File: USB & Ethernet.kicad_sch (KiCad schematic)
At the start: 17 parts

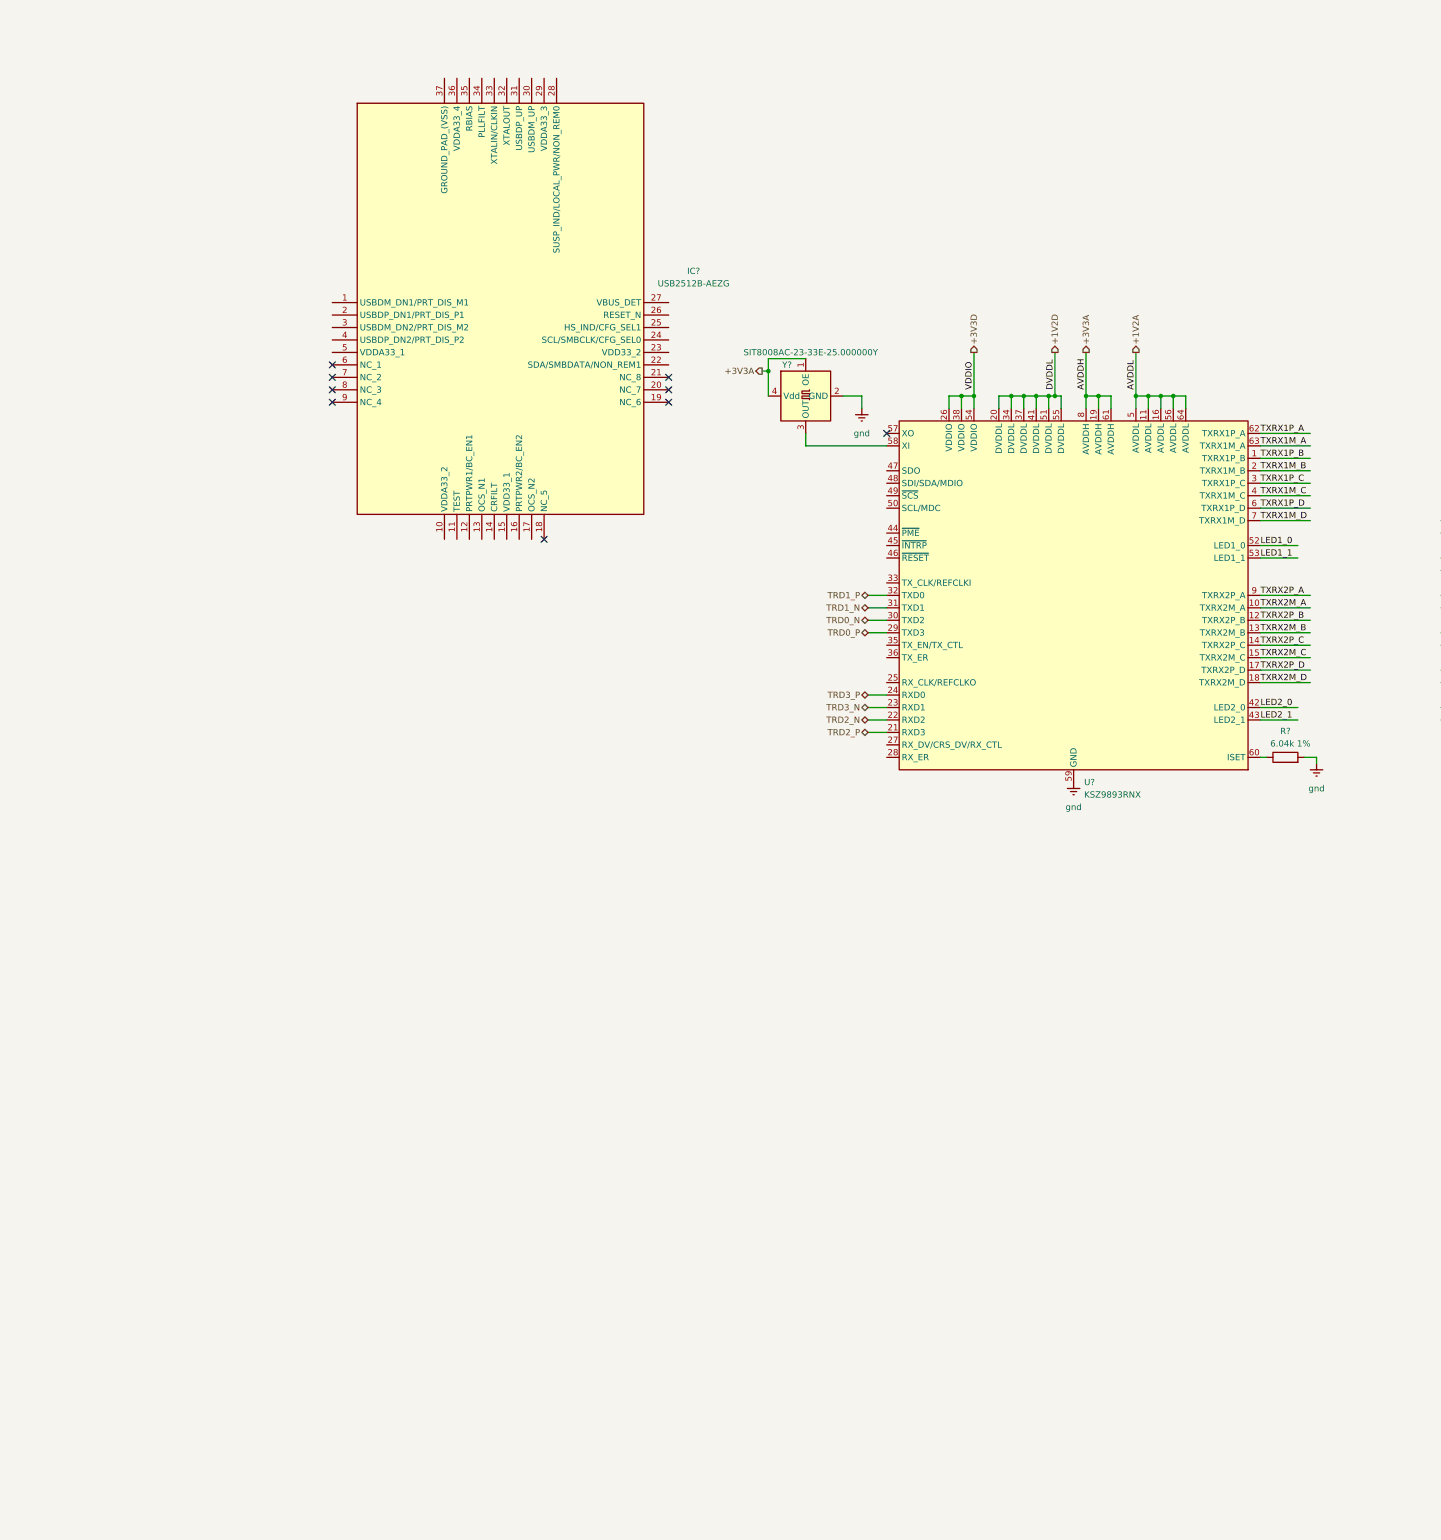
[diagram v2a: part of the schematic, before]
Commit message: switched from KSZ9893RNX to SJA1105PEL for sgmii support
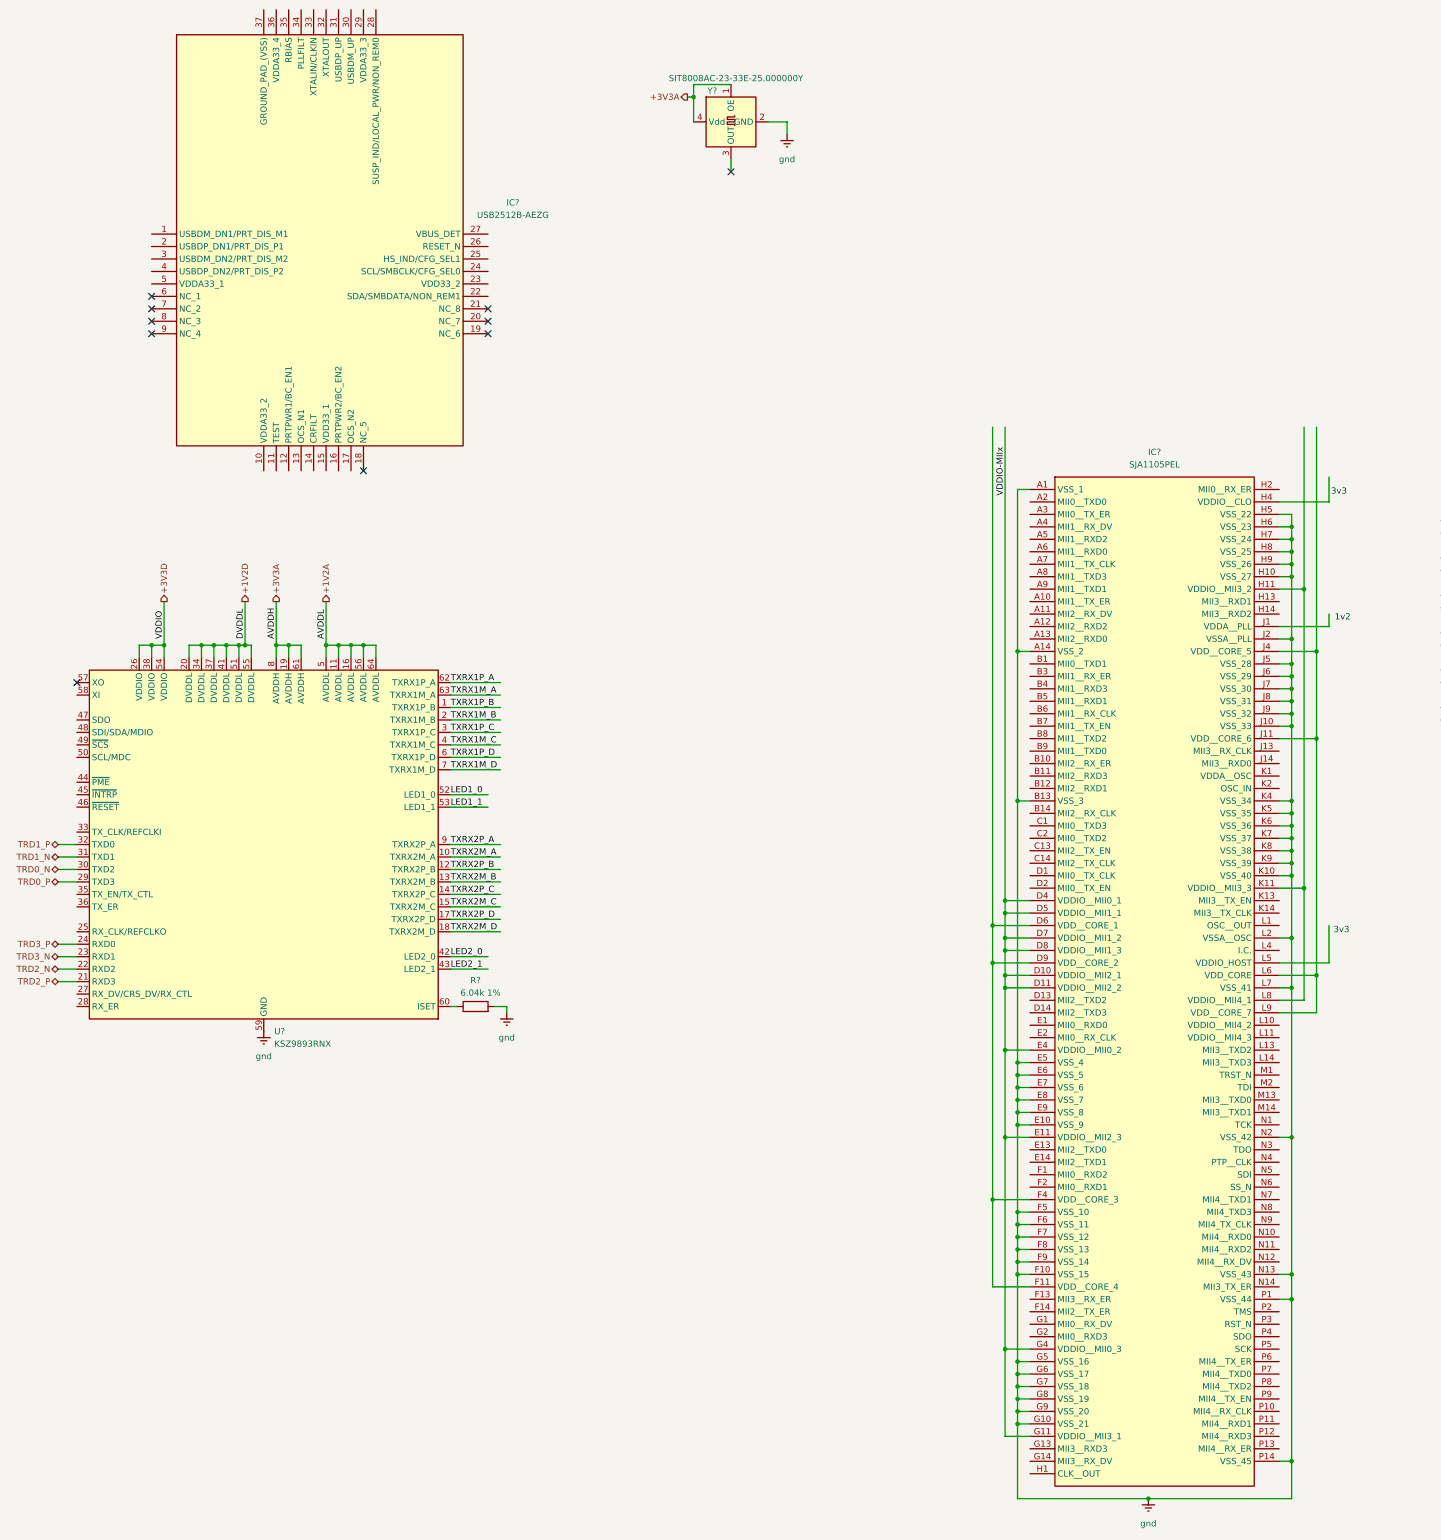
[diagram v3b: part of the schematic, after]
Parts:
- added IC?: SJA1105PEL, BGA159C80P14X14_1200X1200X150, symbol SJA1105PEL:SJA1105PEL
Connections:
- net gnd: now also IC?.A1 (VSS_1), IC?.A14 (VSS_2), IC?.B13 (VSS_3), IC?.E10 (VSS_9), IC?.E5 (VSS_4), IC?.E6 (VSS_5), IC?.E7 (VSS_6), IC?.E8 (VSS_7), IC?.E9 (VSS_8), IC?.F10 (VSS_15), IC?.F5 (VSS_10), IC?.F6 (VSS_11), IC?.F7 (VSS_12), IC?.F8 (VSS_13), IC?.F9 (VSS_14), IC?.G10 (VSS_21), IC?.G5 (VSS_16), IC?.G6 (VSS_17), IC?.G7 (VSS_18), IC?.G8 (VSS_19), IC?.G9 (VSS_20), IC?.H10 (VSS_27), IC?.H5 (VSS_22), IC?.H6 (VSS_23), IC?.H7 (VSS_24), IC?.H8 (VSS_25), IC?.H9 (VSS_26), IC?.J10 (VSS_33), IC?.J2 (VSSA__PLL), IC?.J5 (VSS_28), IC?.J6 (VSS_29), IC?.J7 (VSS_30), IC?.J8 (VSS_31), IC?.J9 (VSS_32), IC?.K10 (VSS_40), IC?.K4 (VSS_34), IC?.K5 (VSS_35), IC?.K6 (VSS_36), IC?.K7 (VSS_37), IC?.K8 (VSS_38), IC?.K9 (VSS_39), IC?.L2 (VSSA__OSC), IC?.L7 (VSS_41), IC?.N13 (VSS_43), IC?.N2 (VSS_42), IC?.P1 (VSS_44), IC?.P14 (VSS_45)
- net at U?.58 (XI): no longer Y?.3 (OUT)
- new net: IC?.D6 (VDD__CORE_1), IC?.D9 (VDD__CORE_2), IC?.F11 (VDD__CORE_4), IC?.F4 (VDD__CORE_3)
- new net: IC?.H11 (VDDIO__MII3_2), IC?.K11 (VDDIO__MII3_3), IC?.L8 (VDDIO__MII4_1)
- new net: IC?.J11 (VDD__CORE_6), IC?.J4 (VDD__CORE_5), IC?.L6 (VDD_CORE), IC?.L9 (VDD__CORE_7)
- new net VDDIO-MIIx: IC?.D10 (VDDIO__MII2_1), IC?.D11 (VDDIO__MII2_2), IC?.D4 (VDDIO__MII0_1), IC?.D5 (VDDIO__MII1_1), IC?.D7 (VDDIO__MII1_2), IC?.D8 (VDDIO__MII1_3), IC?.E11 (VDDIO__MII2_3), IC?.E4 (VDDIO__MII0_2), IC?.G11 (VDDIO__MII3_1), IC?.G4 (VDDIO__MII0_3)
- no-connect marks 9 -> 10
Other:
- note added: "1v2"
- note added: "3v3"
- moved on the sheet: IC?, R?, U?, Y?

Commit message: Swiitched to JSM561
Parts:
- added J?: JXD0-4015NL, JXD0-4015NL_PUL, symbol JXD0-4015NL:JXD0-4015NL
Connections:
- net SYNC_OUT: now reaches IC?.N4 (PTP__CLK)
- net gnd: no longer names the net of IC?.A1 (VSS_1), IC?.A14 (VSS_2), IC?.B13 (VSS_3), IC?.E10 (VSS_9), IC?.E5 (VSS_4), IC?.E6 (VSS_5), IC?.E7 (VSS_6), IC?.E8 (VSS_7), IC?.E9 (VSS_8), IC?.F10 (VSS_15), IC?.F5 (VSS_10), IC?.F6 (VSS_11), IC?.F7 (VSS_12), IC?.F8 (VSS_13), IC?.F9 (VSS_14), IC?.G10 (VSS_21), IC?.G5 (VSS_16), IC?.G6 (VSS_17), IC?.G7 (VSS_18), IC?.G8 (VSS_19), IC?.G9 (VSS_20), IC?.H10 (VSS_27), IC?.H5 (VSS_22), IC?.H6 (VSS_23), IC?.H7 (VSS_24), IC?.H8 (VSS_25), IC?.H9 (VSS_26), IC?.J10 (VSS_33), IC?.J2 (VSSA__PLL), IC?.J5 (VSS_28), IC?.J6 (VSS_29), IC?.J7 (VSS_30), IC?.J8 (VSS_31), IC?.J9 (VSS_32), IC?.K10 (VSS_40), IC?.K4 (VSS_34), IC?.K5 (VSS_35), IC?.K6 (VSS_36), IC?.K7 (VSS_37), IC?.K8 (VSS_38), IC?.K9 (VSS_39), IC?.L2 (VSSA__OSC), IC?.L7 (VSS_41), IC?.N13 (VSS_43), IC?.N2 (VSS_42), IC?.P1 (VSS_44), IC?.P14 (VSS_45)
- net gnd: no longer C?.2, C?.2, C?.2, C?.2, C?.2, C?.2, C?.2, C?.2, J?.MH1, J?.MH2, J?.MH3, J?.MH4, R?.2, U?.59 (GND), U?.65 (GND), Y?.2 (GND)
- new net: C?.2, C?.2, C?.2, C?.2, C?.2, C?.2, C?.2, C?.2
- new net: U?.59 (GND), U?.65 (GND)
- new net: J?.MH1, J?.MH2, J?.MH3, J?.MH4
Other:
- moved on the sheet: C?, R?

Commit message: Removed Ethernet
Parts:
- removed C? (x8): 0.1u, symbol Device:C_Small
- removed IC?: USB2512B-AEZG, QFN50P600X600X100-37N-D, symbol USB2512B-AEZG:USB2512B-AEZG
- removed IC?: SJA1105PEL, BGA159C80P14X14_1200X1200X150, symbol SJA1105PEL:SJA1105PEL
- removed J?: JXD0-4015NL, JXD0-4015NL_PUL, symbol JXD0-4015NL:JXD0-4015NL
- removed J?: RJMG212S21130ER, RJMG212S21130ER, symbol RJMG212S21130ER:RJMG212S21130ER
- removed R? (x4): 330R, Resistor_SMD:R_0402_1005Metric, symbol Device:R
- removed R?: 6.04k 1%, symbol Device:R
- removed U?: KSZ9893RNX, Package_DFN_QFN:QFN-64-1EP_8x8mm_P0.4mm_EP6.5x6.5mm, symbol Interface_Ethernet:KSZ9893RNX
- removed Y?: SIT8008AC-23-33E-25.000000Y, Oscillator:Oscillator_SMD_SiT_PQFN-4Pin_3.2x2.5mm, symbol Oscillator:SiT8008xx-2x-xxE
- added IC?: USB2512B-AEZG, QFN50P600X600X100-37N-D, symbol USB2512B-AEZG:USB2512B-AEZG
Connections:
- new net: IC?.10 (VDDA33_2), IC?.15 (VDD33_1), IC?.23 (VDD33_2), IC?.36 (VDDA33_4), IC?.5 (VDDA33_1)
- no-connect marks 10 -> 8
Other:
- note removed: "1v2"
- note removed: "3v3"

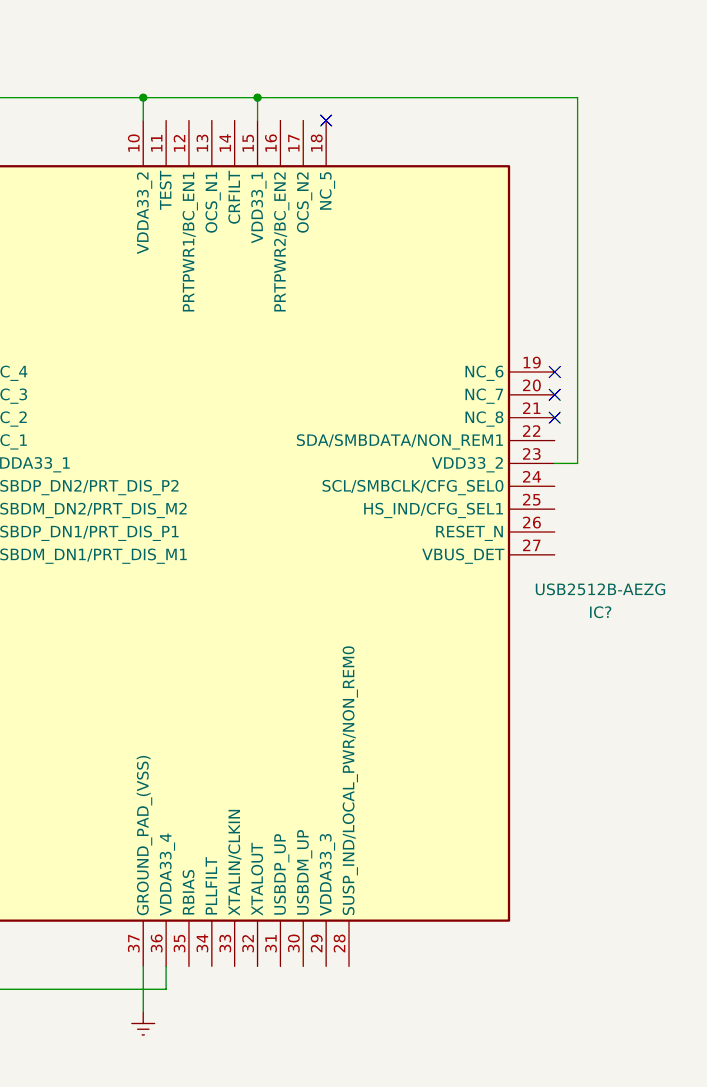
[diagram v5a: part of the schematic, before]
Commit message: Sheets neatened
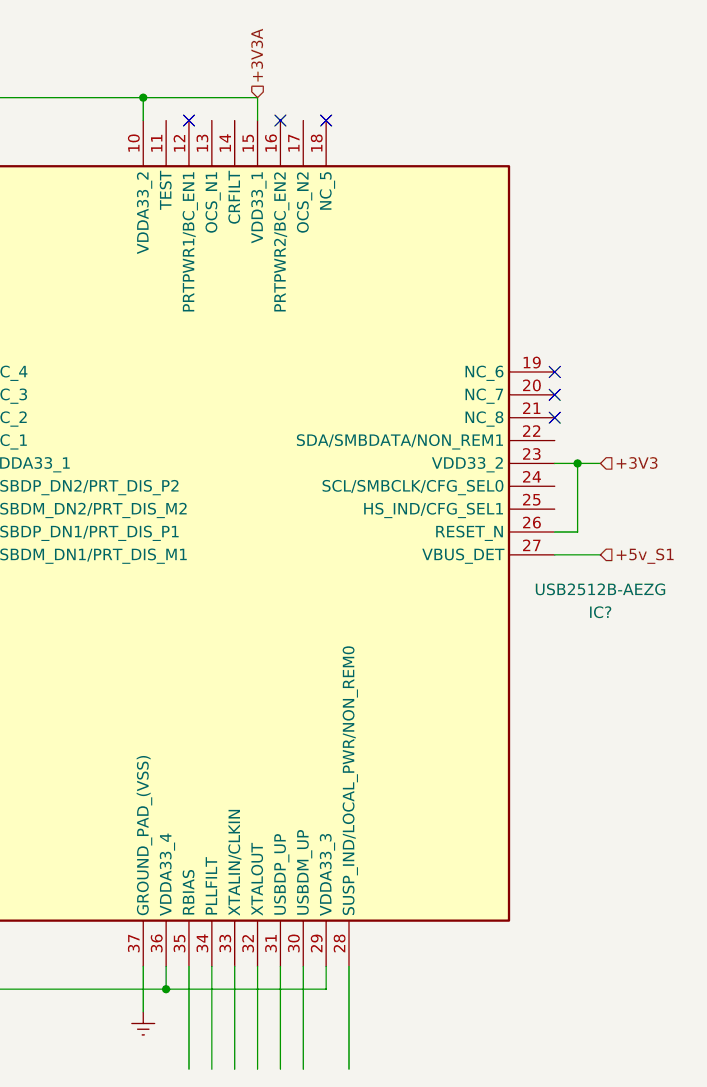
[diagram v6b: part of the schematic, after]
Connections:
- net +3V3A: now reaches IC?.10 (VDDA33_2), IC?.15 (VDD33_1), IC?.36 (VDDA33_4), IC?.5 (VDDA33_1)
- net +3V3A: now also IC?.29 (VDDA33_3); no longer IC?.23 (VDD33_2)
- net +3V3: now reaches IC?.26 (RESET_N)
- net +3V3: now also IC?.23 (VDD33_2)
- net +5v_S1: now reaches IC?.27 (VBUS_DET)
- no-connect marks 8 -> 10
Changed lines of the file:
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@@
+	)
+	(junction
+		(at 186.69 74.93)
+		(diameter 0)
+		(color 0 0 0 0)
 	)
 	(junction
@@
 	)
 	(junction
-		(at 151.13 34.29)
+		(at 140.97 133.35)
 		(diameter 0)
 		(color 0 0 0 0)
@@
 	)
 	(no_connect
+		(at 153.67 36.83)
+	)
+	(no_connect
 		(at 184.15 69.85)
 	)
@@
 	)
 	(no_connect
+		(at 143.51 36.83)
+	)
+	(no_connect
 		(at 115.57 72.39)
 	)
@@
 	(wire
 		(pts
+			(xy 184.15 82.55) (xy 186.69 82.55)
+		)
+		(stroke
+			(width 0)
+			(type default)
+		)
+	)
+	(wire
+		(pts
 			(xy 113.03 133.35) (xy 113.03 74.93)
 		)
@@
 	(wire
 		(pts
+			(xy 140.97 133.35) (xy 158.75 133.35)
+		)
+		(stroke
+			(width 0)
+			(type default)
+		)
+	)
+	(wire
+		(pts
+			(xy 153.67 130.81) (xy 153.67 142.24)
+		)
+		(stroke
+			(width 0)
+			(type default)
+		)
+	)
+	(wire
+		(pts
 			(xy 138.43 130.81) (xy 138.43 135.89)
 		)
@@
 	(wire
 		(pts
+			(xy 186.69 74.93) (xy 189.23 74.93)
+		)
+		(stroke
+			(width 0)
+			(type default)
+		)
+	)
+	(wire
+		(pts
 			(xy 138.43 36.83) (xy 138.43 34.29)
 		)
@@
 	(wire
 		(pts
+			(xy 156.21 130.81) (xy 156.21 142.24)
+		)
+		(stroke
+			(width 0)
+			(type default)
+		)
+	)
+	(wire
+		(pts
+			(xy 184.15 85.09) (xy 189.23 85.09)
+		)
+		(stroke
+			(width 0)
+			(type default)
+		)
+	)
+	(wire
+		(pts
 			(xy 138.43 34.29) (xy 151.13 34.29)
 		)
@@
 	(wire
 		(pts
-			(xy 186.69 74.93) (xy 186.69 34.29)
+			(xy 146.05 130.81) (xy 146.05 142.24)
+		)
+		(stroke
+			(width 0)
+			(type default)
+		)
+	)
+	(wire
+		(pts
+			(xy 161.29 130.81) (xy 161.29 142.24)
+		)
+		(stroke
+			(width 0)
+			(type default)
+		)
+	)
+	(wire
+		(pts
+			(xy 186.69 82.55) (xy 186.69 74.93)
 		)
 		(stroke
@@
 	(wire
 		(pts
-			(xy 151.13 34.29) (xy 186.69 34.29)
+			(xy 151.13 130.81) (xy 151.13 142.24)
+		)
+		(stroke
+			(width 0)
+			(type default)
+		)
+	)
+	(wire
+		(pts
+			(xy 148.59 130.81) (xy 148.59 142.24)
 		)
 		(stroke
@@
 		)
 	)
+	(wire
+		(pts
+			(xy 158.75 130.81) (xy 158.75 133.35)
+		)
+		(stroke
+			(width 0)
+			(type default)
+		)
+	)
+	(wire
+		(pts
+			(xy 143.51 130.81) (xy 143.51 142.24)
+		)
+		(stroke
+			(width 0)
+			(type default)
+		)
+	)
+	(hierarchical_label "+5v_S1"
+		(shape input)
+		(at 189.23 85.09 0)
+		(effects
+			(font
+				(size 1.27 1.27)
+			)
+			(justify left)
+		)
+	)
+	(hierarchical_label "+3V3A"
+		(shape input)
+		(at 151.13 34.29 90)
+		(effects
+			(font
+				(size 1.27 1.27)
+			)
+			(justify left)
+		)
+	)
+	(hierarchical_label "+3V3"
+		(shape input)
+		(at 189.23 74.93 0)
+		(effects
+			(font
+				(size 1.27 1.27)
+			)
+			(justify left)
+		)
+	)
